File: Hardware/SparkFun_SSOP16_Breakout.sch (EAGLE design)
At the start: 4 parts, among them U1 SSOP16

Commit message: Updated board files
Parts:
- removed U$1: LOGO-SFESK, SparkFun:LOGO-SFESK
- added FRAME1: FRAME-LETTER, SparkFun-Aesthetics:FRAME-LETTER
- added LOGO1: SFE_LOGO_FLAME.1_INCH, SparkFun-Aesthetics:SFE_LOGO_FLAME.1_INCH
- added LOGO3: OSHW-LOGOS, SparkFun-Aesthetics:OSHW-LOGOS
- JP1: device SparkFun:M08 -> SparkFun-Connectors:M08NO_SILK
- JP2: device SparkFun:M08 -> SparkFun-Connectors:M08NO_SILK_FEMALE_PTH
- U1: device SparkFun:SSOP16 -> generic-ssop16:SSOP16
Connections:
- net N$1: now also U1.1; no longer U1.P$8
- net N$10: now also U1.15; no longer U1.P$15
- net N$11: now also U1.14; no longer U1.P$14
- net N$12: now also U1.13; no longer U1.P$13
- net N$13: now also U1.12; no longer U1.P$12
- net N$14: now also U1.11; no longer U1.P$11
- net N$15: now also U1.10; no longer U1.P$10
- net N$16: now also U1.9; no longer U1.P$9
- net N$2: now also U1.2; no longer U1.P$7
- net N$3: now also U1.3; no longer U1.P$6
- net N$4: now also U1.4; no longer U1.P$5
- net N$5: now also U1.5; no longer U1.P$4
- net N$6: now also U1.6; no longer U1.P$3
- net N$7: now also U1.7; no longer U1.P$2
- net N$8: now also U1.8; no longer U1.P$1
- net N$9: now also U1.16; no longer U1.P$16
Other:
- note added: "Byron Jacquot"
- note added: "V20"
- moved on the sheet: JP1

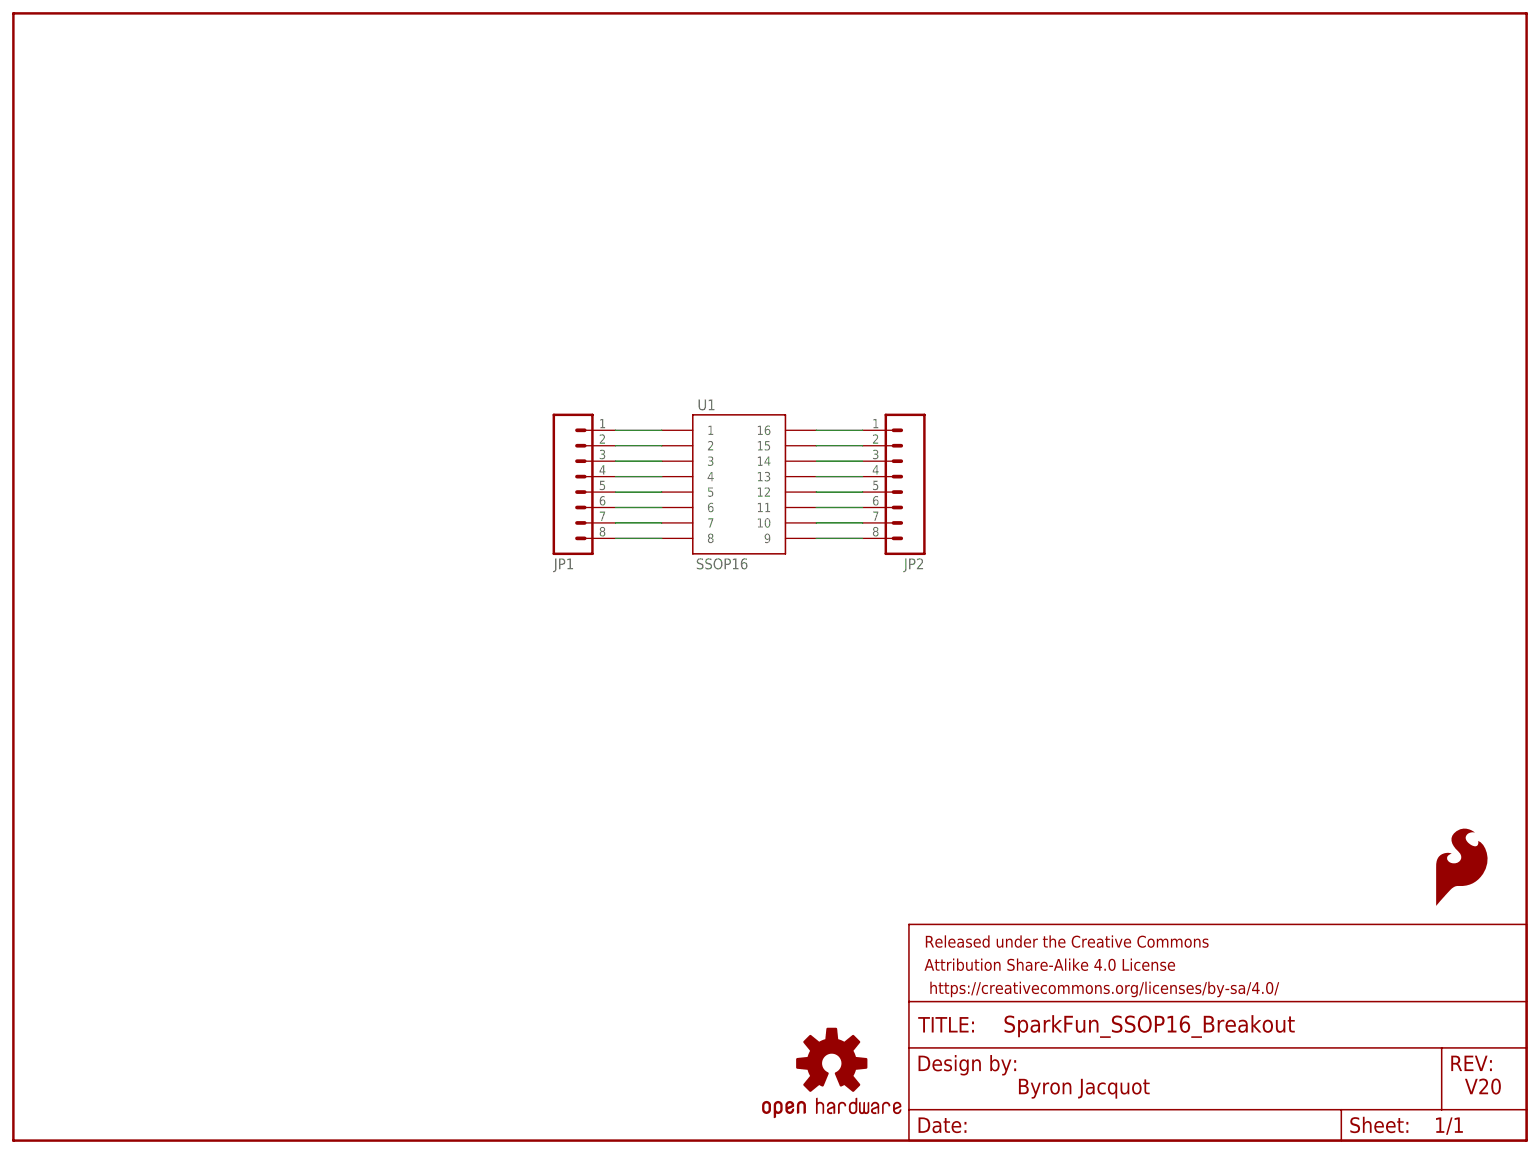
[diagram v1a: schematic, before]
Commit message: Moving towards actual design.
-2-up panel.
-Dimensioning added.
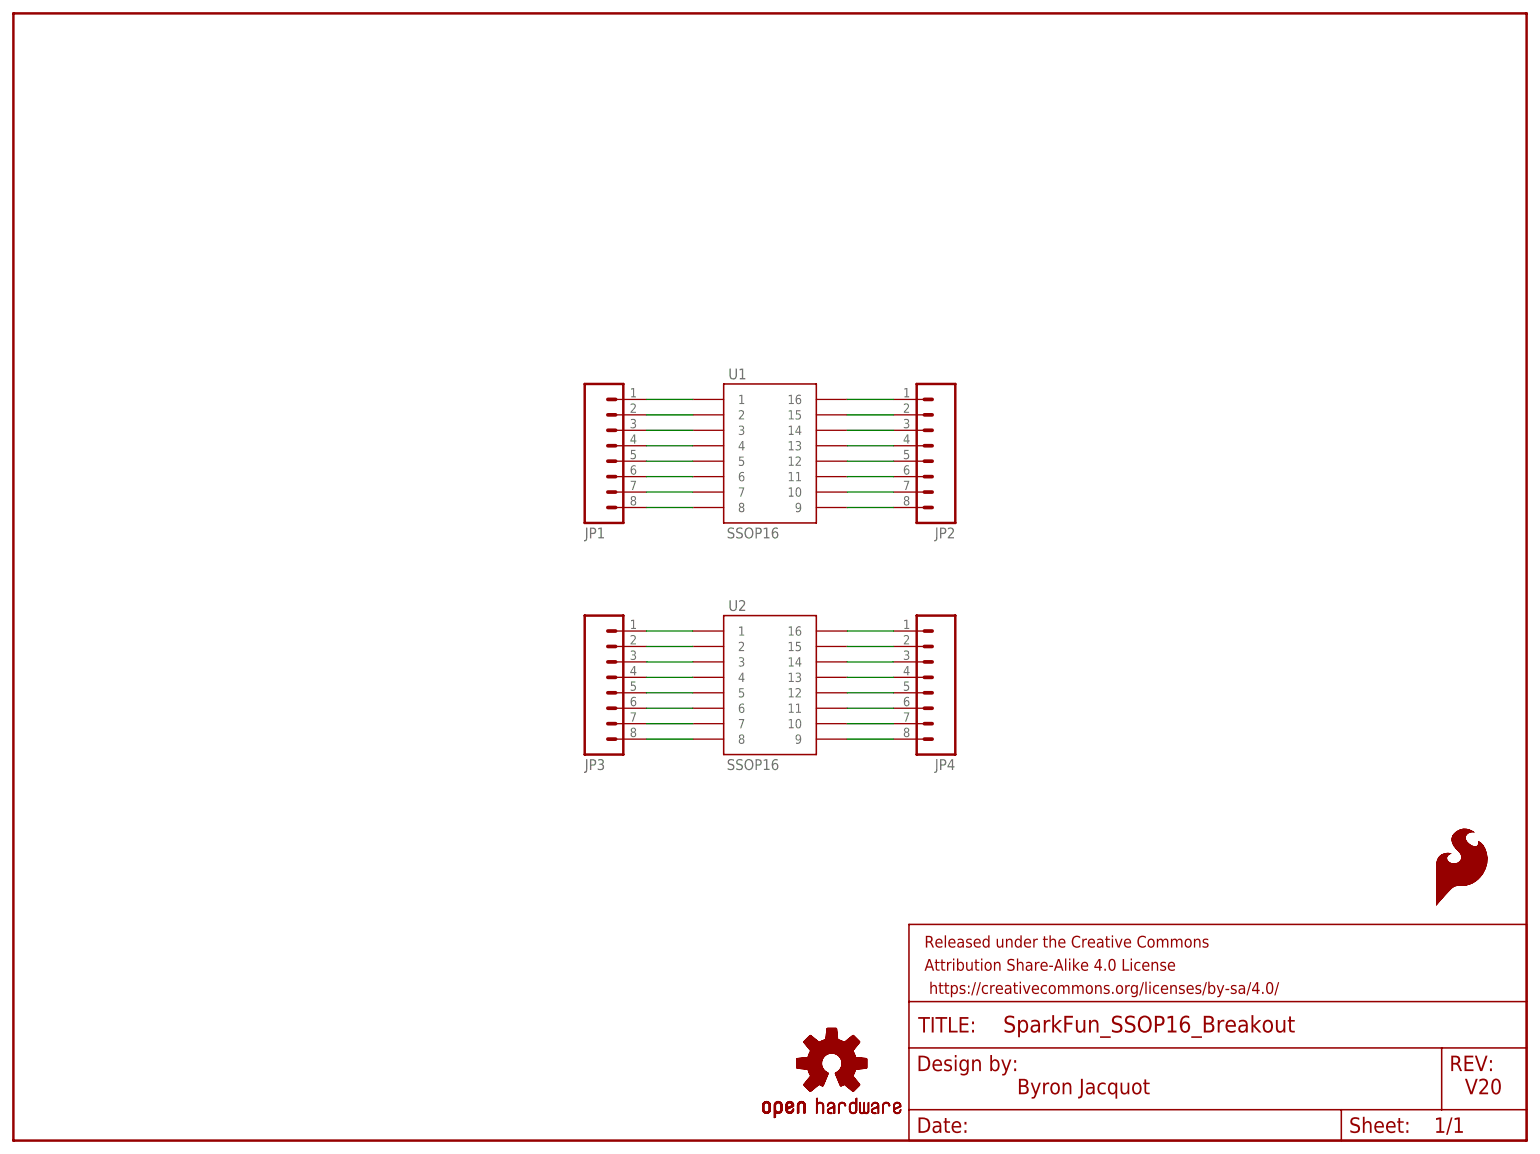
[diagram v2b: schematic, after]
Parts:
- added JP3: (no value), SparkFun-Connectors:M08NO_SILK
- added JP4: (no value), SparkFun-Connectors:M08NO_SILK_FEMALE_PTH
- added LOGO2: SFE_LOGO_FLAME.1_INCH, SparkFun-Aesthetics:SFE_LOGO_FLAME.1_INCH
- added LOGO4: OSHW-LOGOS, SparkFun-Aesthetics:OSHW-LOGOS
- added U2: SSOP16, generic-ssop16:SSOP16
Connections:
- new net N$17: JP4.1, U2.16
- new net N$18: JP4.2, U2.15
- new net N$19: JP4.3, U2.14
- new net N$20: JP4.4, U2.13
- new net N$21: JP4.5, U2.12
- new net N$22: JP4.6, U2.11
- new net N$23: JP4.7, U2.10
- new net N$24: JP4.8, U2.9
- new net N$25: JP3.1, U2.1
- new net N$26: JP3.2, U2.2
- new net N$27: JP3.3, U2.3
- new net N$28: JP3.4, U2.4
- new net N$29: JP3.5, U2.5
- new net N$30: JP3.6, U2.6
- new net N$31: JP3.7, U2.7
- new net N$32: JP3.8, U2.8
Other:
- moved on the sheet: JP1, JP2, U1
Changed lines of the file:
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@@
 <part name="LOGO1" library="SparkFun-Aesthetics" deviceset="SFE_LOGO_FLAME" device=".1_INCH"/>
 <part name="LOGO3" library="SparkFun-Aesthetics" deviceset="OSHW-LOGO" device="S"/>
+<part name="U2" library="generic-ssop16" deviceset="SSOP16" device=""/>
+<part name="JP3" library="SparkFun-Connectors" deviceset="M08" device="NO_SILK"/>
+<part name="JP4" library="SparkFun-Connectors" deviceset="M08" device="NO_SILK_FEMALE_PTH"/>
+<part name="LOGO2" library="SparkFun-Aesthetics" deviceset="SFE_LOGO_FLAME" device=".1_INCH"/>
+<part name="LOGO4" library="SparkFun-Aesthetics" deviceset="OSHW-LOGO" device="S"/>
 </parts>
 <sheets>
@@
 </plain>
 <instances>
-<instance part="U1" gate="G$1" x="119.38" y="109.22"/>
-<instance part="JP1" gate="G$1" x="93.98" y="109.22" rot="MR180"/>
-<instance part="JP2" gate="G$1" x="144.78" y="109.22" rot="R180"/>
+<instance part="U1" gate="G$1" x="124.46" y="114.3"/>
+<instance part="JP1" gate="G$1" x="99.06" y="114.3" rot="MR180"/>
+<instance part="JP2" gate="G$1" x="149.86" y="114.3" rot="R180"/>
 <instance part="FRAME1" gate="G$1" x="0" y="0"/>
 <instance part="FRAME1" gate="V" x="147.32" y="0"/>
 <instance part="LOGO1" gate="G$1" x="233.68" y="38.1"/>
 <instance part="LOGO3" gate="G$1" x="134.62" y="12.7"/>
+<instance part="U2" gate="G$1" x="124.46" y="76.2"/>
+<instance part="JP3" gate="G$1" x="99.06" y="76.2" rot="MR180"/>
+<instance part="JP4" gate="G$1" x="149.86" y="76.2" rot="R180"/>
+<instance part="LOGO2" gate="G$1" x="233.68" y="38.1"/>
+<instance part="LOGO4" gate="G$1" x="134.62" y="12.7"/>
 </instances>
 <busses>
@@
 <net name="N$9" class="0">
 <segment>
-<wire x1="139.7" y1="116.84" x2="132.08" y2="116.84" width="0.1524" layer="91"/>
+<wire x1="144.78" y1="121.92" x2="137.16" y2="121.92" width="0.1524" layer="91"/>
 <pinref part="U1" gate="G$1" pin="16"/>
 <pinref part="JP2" gate="G$1" pin="1"/>
@@
 <net name="N$10" class="0">
 <segment>
-<wire x1="139.7" y1="114.3" x2="132.08" y2="114.3" width="0.1524" layer="91"/>
+<wire x1="144.78" y1="119.38" x2="137.16" y2="119.38" width="0.1524" layer="91"/>
 <pinref part="U1" gate="G$1" pin="15"/>
 <pinref part="JP2" gate="G$1" pin="2"/>
@@
 <net name="N$11" class="0">
 <segment>
-<wire x1="139.7" y1="111.76" x2="132.08" y2="111.76" width="0.1524" layer="91"/>
+<wire x1="144.78" y1="116.84" x2="137.16" y2="116.84" width="0.1524" layer="91"/>
 <pinref part="U1" gate="G$1" pin="14"/>
 <pinref part="JP2" gate="G$1" pin="3"/>
@@
 <net name="N$12" class="0">
 <segment>
-<wire x1="139.7" y1="109.22" x2="132.08" y2="109.22" width="0.1524" layer="91"/>
+<wire x1="144.78" y1="114.3" x2="137.16" y2="114.3" width="0.1524" layer="91"/>
 <pinref part="U1" gate="G$1" pin="13"/>
 <pinref part="JP2" gate="G$1" pin="4"/>
@@
 <net name="N$13" class="0">
 <segment>
-<wire x1="139.7" y1="106.68" x2="132.08" y2="106.68" width="0.1524" layer="91"/>
+<wire x1="144.78" y1="111.76" x2="137.16" y2="111.76" width="0.1524" layer="91"/>
 <pinref part="U1" gate="G$1" pin="12"/>
 <pinref part="JP2" gate="G$1" pin="5"/>
@@
 <net name="N$14" class="0">
 <segment>
-<wire x1="139.7" y1="104.14" x2="132.08" y2="104.14" width="0.1524" layer="91"/>
+<wire x1="144.78" y1="109.22" x2="137.16" y2="109.22" width="0.1524" layer="91"/>
 <pinref part="U1" gate="G$1" pin="11"/>
 <pinref part="JP2" gate="G$1" pin="6"/>
@@
 <net name="N$15" class="0">
 <segment>
-<wire x1="139.7" y1="101.6" x2="132.08" y2="101.6" width="0.1524" layer="91"/>
+<wire x1="144.78" y1="106.68" x2="137.16" y2="106.68" width="0.1524" layer="91"/>
 <pinref part="U1" gate="G$1" pin="10"/>
 <pinref part="JP2" gate="G$1" pin="7"/>
@@
 <net name="N$16" class="0">
 <segment>
-<wire x1="139.7" y1="99.06" x2="132.08" y2="99.06" width="0.1524" layer="91"/>
+<wire x1="144.78" y1="104.14" x2="137.16" y2="104.14" width="0.1524" layer="91"/>
 <pinref part="U1" gate="G$1" pin="9"/>
 <pinref part="JP2" gate="G$1" pin="8"/>
@@
 <pinref part="U1" gate="G$1" pin="1"/>
 <pinref part="JP1" gate="G$1" pin="1"/>
-<wire x1="99.06" y1="116.84" x2="106.68" y2="116.84" width="0.1524" layer="91"/>
+<wire x1="104.14" y1="121.92" x2="111.76" y2="121.92" width="0.1524" layer="91"/>
 </segment>
 </net>
@@
 <pinref part="U1" gate="G$1" pin="2"/>
 <pinref part="JP1" gate="G$1" pin="2"/>
-<wire x1="99.06" y1="114.3" x2="106.68" y2="114.3" width="0.1524" layer="91"/>
+<wire x1="104.14" y1="119.38" x2="111.76" y2="119.38" width="0.1524" layer="91"/>
 </segment>
 </net>
@@
 <pinref part="U1" gate="G$1" pin="3"/>
 <pinref part="JP1" gate="G$1" pin="3"/>
-<wire x1="99.06" y1="111.76" x2="106.68" y2="111.76" width="0.1524" layer="91"/>
+<wire x1="104.14" y1="116.84" x2="111.76" y2="116.84" width="0.1524" layer="91"/>
 </segment>
 </net>
@@
 <pinref part="U1" gate="G$1" pin="4"/>
 <pinref part="JP1" gate="G$1" pin="4"/>
-<wire x1="99.06" y1="109.22" x2="106.68" y2="109.22" width="0.1524" layer="91"/>
+<wire x1="104.14" y1="114.3" x2="111.76" y2="114.3" width="0.1524" layer="91"/>
 </segment>
 </net>
@@
 <pinref part="U1" gate="G$1" pin="5"/>
 <pinref part="JP1" gate="G$1" pin="5"/>
-<wire x1="99.06" y1="106.68" x2="106.68" y2="106.68" width="0.1524" layer="91"/>
+<wire x1="104.14" y1="111.76" x2="111.76" y2="111.76" width="0.1524" layer="91"/>
 </segment>
 </net>
@@
 <pinref part="U1" gate="G$1" pin="6"/>
 <pinref part="JP1" gate="G$1" pin="6"/>
-<wire x1="99.06" y1="104.14" x2="106.68" y2="104.14" width="0.1524" layer="91"/>
+<wire x1="104.14" y1="109.22" x2="111.76" y2="109.22" width="0.1524" layer="91"/>
 </segment>
 </net>
@@
 <pinref part="U1" gate="G$1" pin="7"/>
 <pinref part="JP1" gate="G$1" pin="7"/>
-<wire x1="99.06" y1="101.6" x2="106.68" y2="101.6" width="0.1524" layer="91"/>
+<wire x1="104.14" y1="106.68" x2="111.76" y2="106.68" width="0.1524" layer="91"/>
 </segment>
 </net>
@@
 <pinref part="U1" gate="G$1" pin="8"/>
 <pinref part="JP1" gate="G$1" pin="8"/>
-<wire x1="99.06" y1="99.06" x2="106.68" y2="99.06" width="0.1524" layer="91"/>
-</segment>
-</net>
+<wire x1="104.14" y1="104.14" x2="111.76" y2="104.14" width="0.1524" layer="91"/>
+</segment>
+</net>
+<net name="N$17" class="0">
+<segment>
+<wire x1="144.78" y1="83.82" x2="137.16" y2="83.82" width="0.1524" layer="91"/>
+<pinref part="U2" gate="G$1" pin="16"/>
+<pinref part="JP4" gate="G$1" pin="1"/>
+</segment>
+</net>
+<net name="N$18" class="0">
+<segment>
+<wire x1="144.78" y1="81.28" x2="137.16" y2="81.28" width="0.1524" layer="91"/>
+<pinref part="U2" gate="G$1" pin="15"/>
+<pinref part="JP4" gate="G$1" pin="2"/>
+</segment>
+</net>
+<net name="N$19" class="0">
+<segment>
+<wire x1="144.78" y1="78.74" x2="137.16" y2="78.74" width="0.1524" layer="91"/>
+<pinref part="U2" gate="G$1" pin="14"/>
+<pinref part="JP4" gate="G$1" pin="3"/>
+</segment>
+</net>
+<net name="N$20" class="0">
+<segment>
+<wire x1="144.78" y1="76.2" x2="137.16" y2="76.2" width="0.1524" layer="91"/>
+<pinref part="U2" gate="G$1" pin="13"/>
+<pinref part="JP4" gate="G$1" pin="4"/>
+</segment>
+</net>
+<net name="N$21" class="0">
+<segment>
+<wire x1="144.78" y1="73.66" x2="137.16" y2="73.66" width="0.1524" layer="91"/>
+<pinref part="U2" gate="G$1" pin="12"/>
+<pinref part="JP4" gate="G$1" pin="5"/>
+</segment>
+</net>
+<net name="N$22" class="0">
+<segment>
+<wire x1="144.78" y1="71.12" x2="137.16" y2="71.12" width="0.1524" layer="91"/>
+<pinref part="U2" gate="G$1" pin="11"/>
+<pinref part="JP4" gate="G$1" pin="6"/>
+</segment>
+</net>
+<net name="N$23" class="0">
+<segment>
+<wire x1="144.78" y1="68.58" x2="137.16" y2="68.58" width="0.1524" layer="91"/>
+<pinref part="U2" gate="G$1" pin="10"/>
+<pinref part="JP4" gate="G$1" pin="7"/>
+</segment>
+</net>
+<net name="N$24" class="0">
+<segment>
+<wire x1="144.78" y1="66.04" x2="137.16" y2="66.04" width="0.1524" layer="91"/>
+<pinref part="U2" gate="G$1" pin="9"/>
+<pinref part="JP4" gate="G$1" pin="8"/>
+</segment>
+</net>
+<net name="N$25" class="0">
+<segment>
+<pinref part="U2" gate="G$1" pin="1"/>
+<pinref part="JP3" gate="G$1" pin="1"/>
+<wire x1="104.14" y1="83.82" x2="111.76" y2="83.82" width="0.1524" layer="91"/>
+</segment>
+</net>
+<net name="N$26" class="0">
+<segment>
+<pinref part="U2" gate="G$1" pin="2"/>
+<pinref part="JP3" gate="G$1" pin="2"/>
+<wire x1="104.14" y1="81.28" x2="111.76" y2="81.28" width="0.1524" layer="91"/>
+</segment>
+</net>
+<net name="N$27" class="0">
+<segment>
+<pinref part="U2" gate="G$1" pin="3"/>
+<pinref part="JP3" gate="G$1" pin="3"/>
+<wire x1="104.14" y1="78.74" x2="111.76" y2="78.74" width="0.1524" layer="91"/>
+</segment>
+</net>
+<net name="N$28" class="0">
+<segment>
+<pinref part="U2" gate="G$1" pin="4"/>
+<pinref part="JP3" gate="G$1" pin="4"/>
+<wire x1="104.14" y1="76.2" x2="111.76" y2="76.2" width="0.1524" layer="91"/>
+</segment>
+</net>
+<net name="N$29" class="0">
+<segment>
+<pinref part="U2" gate="G$1" pin="5"/>
+<pinref part="JP3" gate="G$1" pin="5"/>
+<wire x1="104.14" y1="73.66" x2="111.76" y2="73.66" width="0.1524" layer="91"/>
+</segment>
+</net>
+<net name="N$30" class="0">
+<segment>
+<pinref part="U2" gate="G$1" pin="6"/>
+<pinref part="JP3" gate="G$1" pin="6"/>
+<wire x1="104.14" y1="71.12" x2="111.76" y2="71.12" width="0.1524" layer="91"/>
+</segment>
+</net>
+<net name="N$31" class="0">
+<segment>
+<pinref part="U2" gate="G$1" pin="7"/>
+<pinref part="JP3" gate="G$1" pin="7"/>
+<wire x1="104.14" y1="68.58" x2="111.76" y2="68.58" width="0.1524" layer="91"/>
+</segment>
+</net>
+<net name="N$32" class="0">
+<segment>
+<pinref part="U2" gate="G$1" pin="8"/>
+<pinref part="JP3" gate="G$1" pin="8"/>
+<wire x1="104.14" y1="66.04" x2="111.76" y2="66.04" width="0.1524" layer="91"/>
+</segment>
+</net>
